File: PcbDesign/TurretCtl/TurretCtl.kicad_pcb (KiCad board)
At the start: 4 copper layers, 69.6 x 54.4 mm, 28 parts, among them J1 FLIR, J2 Stepper1, J3 Stepper2, J4 PWR

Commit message: Stepper Control Board V2
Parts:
- added D10: LED, LED_SMD:LED_0603_1608Metric, F.Cu at (29.2, 92.7)
- added D11: LED, LED_SMD:LED_0603_1608Metric, F.Cu at (79.0, 85.3)
- added D12: LED, LED_SMD:LED_0603_1608Metric, F.Cu at (29.2, 89.2)
- added D13: LED, LED_SMD:LED_0603_1608Metric, F.Cu at (79.0, 88.9)
- added D14: LED, LED_SMD:LED_0603_1608Metric, F.Cu at (52.6, 104.6)
- added D15: LED, LED_SMD:LED_0603_1608Metric, F.Cu at (69.1, 69.8)
- added D16: LED, LED_SMD:LED_0603_1608Metric, F.Cu at (29.2, 91.0)
- added D17: LED, LED_SMD:LED_0603_1608Metric, F.Cu at (79.0, 87.1)
- added D18: LED, LED_SMD:LED_0603_1608Metric, F.Cu at (69.1, 72.4)
- added D19: LED, LED_SMD:LED_0603_1608Metric, F.Cu at (69.1, 74.9)
- added D2: LED, LED_SMD:LED_0603_1608Metric, F.Cu at (52.3, 83.8)
- added D3: LED, LED_SMD:LED_0603_1608Metric, F.Cu at (55.6, 94.2)
- added D4: LED, LED_SMD:LED_0603_1608Metric, F.Cu at (52.3, 87.1)
- added D5: LED, LED_SMD:LED_0603_1608Metric, F.Cu at (55.6, 90.9)
- added D6: LED, LED_SMD:LED_0603_1608Metric, F.Cu at (52.3, 90.9)
- added D7: LED, LED_SMD:LED_0603_1608Metric, F.Cu at (55.6, 87.1)
- added D8: LED, LED_SMD:LED_0603_1608Metric, F.Cu at (52.3, 94.2)
- added D9: LED, LED_SMD:LED_0603_1608Metric, F.Cu at (55.6, 83.8)
- added J5: Sensors, Connector_JST:JST_GH_SM06B-GHS-TB_1x06-1MP_P1.25mm_Horizontal, F.Cu at (76.1, 72.5)
- added R10: 330, Resistor_SMD:R_0402_1005Metric, F.Cu at (52.3, 92.5)
- added R11: 330, Resistor_SMD:R_0402_1005Metric, F.Cu at (55.6, 88.6)
- added R12: 330, Resistor_SMD:R_0402_1005Metric, F.Cu at (52.3, 95.8)
- added R13: 330, Resistor_SMD:R_0402_1005Metric, F.Cu at (55.6, 85.3)
- added R14: 330, Resistor_SMD:R_0402_1005Metric, F.Cu at (26.4, 92.7)
- added R15: 330, Resistor_SMD:R_0402_1005Metric, F.Cu at (81.8, 85.3)
- added R16: 330, Resistor_SMD:R_0402_1005Metric, F.Cu at (26.4, 89.2)
- added R17: 330, Resistor_SMD:R_0402_1005Metric, F.Cu at (81.8, 88.9)
- added R18: 330, Resistor_SMD:R_0402_1005Metric, F.Cu at (52.6, 101.1)
- added R19: 330, Resistor_SMD:R_0402_1005Metric, F.Cu at (65.5, 69.8)
- added R20: 330, Resistor_SMD:R_0402_1005Metric, F.Cu at (26.4, 91.0)
- added R21: 330, Resistor_SMD:R_0402_1005Metric, F.Cu at (81.8, 87.1)
- added R22: 330, Resistor_SMD:R_0402_1005Metric, F.Cu at (65.5, 72.4)
- added R23: 330, Resistor_SMD:R_0402_1005Metric, F.Cu at (65.5, 74.9)
- added R6: 330, Resistor_SMD:R_0402_1005Metric, F.Cu at (52.3, 85.3)
- added R7: 330, Resistor_SMD:R_0402_1005Metric, F.Cu at (55.6, 95.8)
- added R8: 330, Resistor_SMD:R_0402_1005Metric, F.Cu at (52.3, 88.6)
- added R9: 330, Resistor_SMD:R_0402_1005Metric, F.Cu at (55.6, 92.5)
- R5: value 290 -> 330
- moved C15 98.9 mm to (36.1, 75.4)
- moved J1 97.7 mm to (46.9, 72.3)
- moved R1 73.5 mm to (26.9, 85.6), turned to 90 degrees
- moved C7 71.1 mm to (42.8, 103.1), turned to 180 degrees
- moved J3 70.7 mm to (61.0, 83.8), turned to -90 degrees
- moved R2 70.4 mm to (28.2, 85.6), turned to -90 degrees
- moved C8 66.6 mm to (30.7, 85.6), turned to 90 degrees
- moved C3 66.2 mm to (39.4, 94.3), turned to 180 degrees
- moved J2 65.7 mm to (47.0, 94.3), turned to 90 degrees
- moved U2 64.6 mm to (35.6, 89.2), turned to 180 degrees
- moved C9 63.8 mm to (32.5, 83.6), turned to 90 degrees
- moved C4 62.5 mm to (40.7, 92.2), turned to 180 degrees
- moved C6 62.5 mm to (40.7, 91.0)
- moved C11 57.9 mm to (67.4, 93.3), turned to -90 degrees
- moved C1 57.2 mm to (68.8, 83.8)
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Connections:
- U1 pad 17: /Stepper2/DVDD -> +5V
- U1 pad 18: /Stepper2/DVDD -> +5V
- U1 pad 25: GND -> (no net)
- U2 pad 17: /Stepper1/DVDD -> +5V
- U2 pad 18: /Stepper1/DVDD -> +5V
- U2 pad 25: GND -> (no net)
- XA1 pad D6: unconnected-(XA1-PadD6) -> D6
- XA1 pad D7: unconnected-(XA1-PadD7) -> D7
- XA1 pad D8: unconnected-(XA1-PadD8) -> D8
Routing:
- net +5V: track 33.9 -> 176.6 mm, vias 0 -> 12
- net SCL: track 72.9 -> 10.5 mm, vias 1 -> 0
- net SDA: track 70.4 -> 9.09 mm, vias 1 -> 0
- net GND: track 36.9 -> 67.2 mm, vias 36 -> 41
- net D8: track 0.00 -> 25.2 mm
- net D7: track 0.00 -> 24.4 mm
- net S2_DIR: track 43.5 -> 28.0 mm, vias 0 -> 1
- net S2_STEP: track 42.5 -> 30.4 mm, vias 0 -> 1
- net D6: track 0.00 -> 11.5 mm
- net /Stepper1/DVDD: track 23.7 -> 33.2 mm, vias 3 -> 0
- net /Stepper2/DVDD: track 23.7 -> 33.0 mm, vias 3 -> 0
- net +12V: track 21.5 -> 30.2 mm
- net S1_STEP: track 59.2 -> 56.0 mm, vias 0 -> 1
- net /Stepper2/RREF: track 3.58 -> 6.36 mm
- net /Stepper1/RREF: track 3.58 -> 6.36 mm
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- added copper zone on B.Cu, net +5V
- added copper zone on F.Cu, net +5V
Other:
- board size 69.6 x 54.4 mm -> 70.4 x 53.8 mm
- board text added: "12V"
- board text added: "5V"
- board text added: "DVDD ENABLE SLEEP"
- board text added: "GND"
- board text added: "LIDAR"
- board text added: "SLEEP ENABLE DVDD"
- board text added: "Sensor1"
- board text added: "Sensor2"
- board text added: "Sensor3"
- board text added: "Sensors"
- board text added: "Stepper Control Board V2 JLCJLCJLCJLC"
- board text added: "s1dir"
- board text added: "s1step"
- board text added: "s2dir"
- board text added: "s2step"
- board text removed: "-"
- board text removed: "A1A2B2B1"
- board text removed: "JLCJLCJLCJLC"
- board text removed: "PWR"
- board text removed: "SCL"
- board text removed: "SDA"
- board text removed: "Sense"
- board text removed: "Stepper Control Board V1"
- board text removed: "V12"

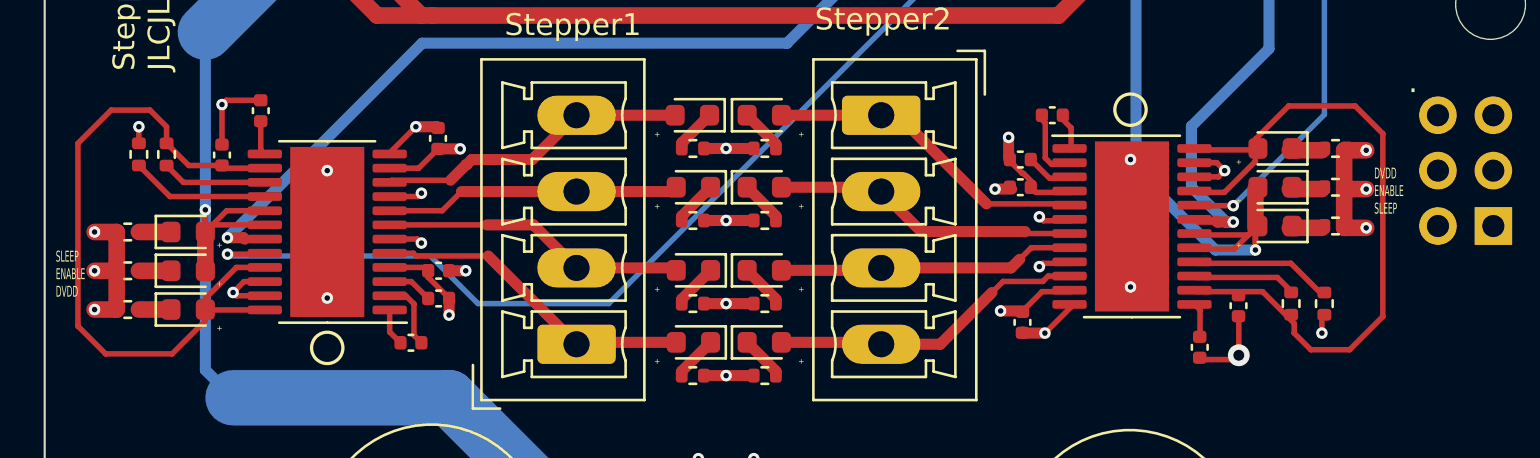
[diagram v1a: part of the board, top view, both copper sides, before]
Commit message: Removed dvdd leds
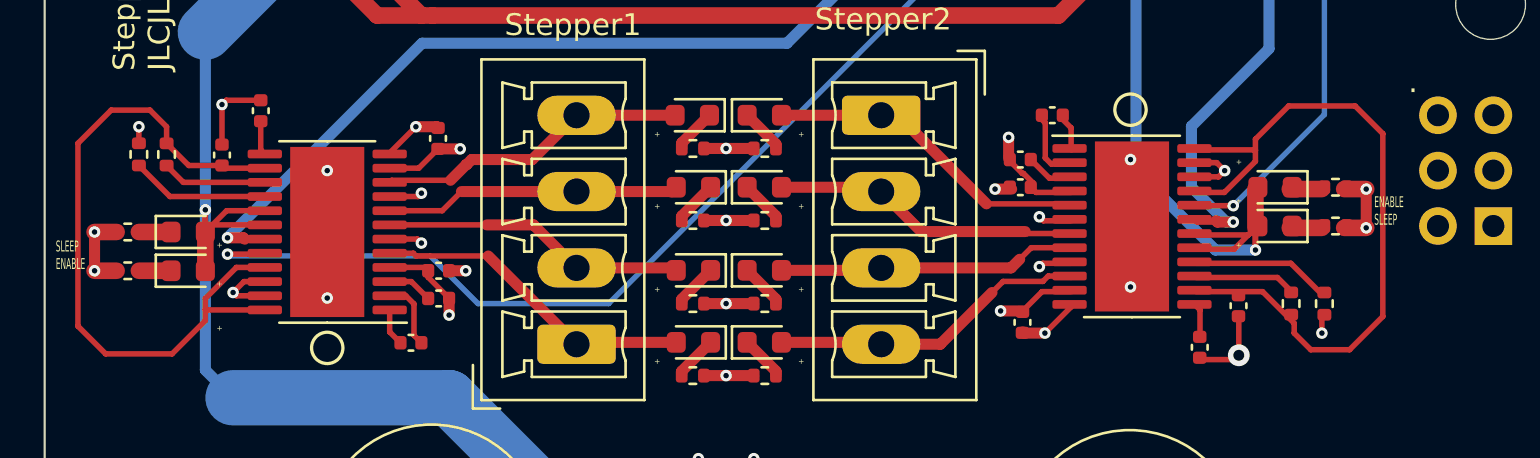
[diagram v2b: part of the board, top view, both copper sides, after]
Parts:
- removed D10, D11: LED, LED_SMD:LED_0603_1608Metric
- removed R14, R15: 330, Resistor_SMD:R_0402_1005Metric
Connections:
- U2 pad 25: (no net) -> GND
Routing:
- net GND: track 67.2 -> 61.6 mm, vias 41 -> 43
- net Net-(D11-K): track 1.47 -> 0.00 mm
- net Net-(D10-K): track 1.47 -> 0.00 mm
- net +5V: vias 12 -> 10
- net (no net): vias 2 -> 0
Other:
- board text added: "ENABLE SLEEP"
- board text added: "SLEEP ENABLE"
- board text removed: "DVDD ENABLE SLEEP"
- board text removed: "SLEEP ENABLE DVDD"

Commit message: New connectors
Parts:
- added D10: LED, LED_SMD:LED_0603_1608Metric, F.Cu at (93.6, 58.3)
- added D11: LED, LED_SMD:LED_0603_1608Metric, F.Cu at (93.6, 60.9)
- added D20: LED, LED_SMD:LED_0603_1608Metric, F.Cu at (93.6, 63.5)
- added R14: 330, Resistor_SMD:R_0402_1005Metric, F.Cu at (97.0, 58.0)
- added R15: 330, Resistor_SMD:R_0402_1005Metric, F.Cu at (97.0, 60.0)
- added R24: 330, Resistor_SMD:R_0402_1005Metric, F.Cu at (97.0, 62.0)
- J1, J5: footprint Connector_JST:JST_GH_SM06B-GHS-TB_1x06-1MP_P1.25mm_Horizontal -> Connector_Phoenix_MC:PhoenixContact_MCV_1,5_6-G-3.5_1x06_P3.50mm_Vertical
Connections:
- U2 pad 25: GND -> (no net)

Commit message: New Layout
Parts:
- moved C9 103.4 mm to (125.9, 128.0), turned to 0 degrees
- moved C8 103.4 mm to (125.9, 126.0), turned to 0 degrees
- moved D16 101.7 mm to (122.5, 131.4)
- moved D12 101.4 mm to (122.5, 128.8)
- moved R20 101.3 mm to (119.0, 132.1), turned to 0 degrees
- moved R16 101.2 mm to (119.0, 130.1), turned to 0 degrees
- moved J2 97.9 mm to (144.8, 89.2)
- moved R1 97.6 mm to (119.0, 118.2), turned to 0 degrees
- moved R2 97.1 mm to (119.0, 120.2), turned to 0 degrees
- moved D9 93.5 mm to (122.5, 149.2)
- moved C5 93.0 mm to (125.9, 122.1), turned to 0 degrees
- moved D20 92.3 mm to (102.9, 155.3)
- moved C6 91.4 mm to (125.9, 124.1)
- moved R13 91.3 mm to (119.0, 151.1), turned to 0 degrees
- moved C4 89.7 mm to (125.9, 120.1), turned to 0 degrees
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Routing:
- net +5V: track 176.6 -> 3.18 mm, vias 10 -> 1
- net S1_DIR: track 60.6 -> 0.00 mm, vias 1 -> 0
- net S1_STEP: track 56.0 -> 0.00 mm, vias 1 -> 0
- net GND: track 61.6 -> 13.4 mm, vias 43 -> 5
- net /Stepper1/DVDD: track 33.2 -> 0.00 mm
- net S2_STEP: track 30.4 -> 1.48 mm
- net S2_DIR: track 28.0 -> 1.47 mm
- net D8: track 25.2 -> 0.00 mm
- net D7: track 24.4 -> 0.00 mm
- net +12V: track 30.2 -> 9.79 mm, vias 13 -> 1
- net S1_AOUT2: track 15.5 -> 0.00 mm
- net S1_AOUT1: track 14.9 -> 0.00 mm
- net S1_BOUT1: track 14.4 -> 0.00 mm
- net S2_AOUT2: track 15.6 -> 1.48 mm, vias 0 -> 1
- net /Stepper2/DVDD: track 33.0 -> 19.0 mm, vias 0 -> 4
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- removed copper zone on F.Cu, net +12V
- removed copper zone on B.Cu, net +5V
- removed copper zone on F.Cu, net +5V
- removed copper zone on F.Cu, net GND
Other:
- board outline removed
- board text removed: "+"
- board text removed: "12V"
- board text removed: "5V"
- board text removed: "ENABLE SLEEP"
- board text removed: "GND"
- board text removed: "LIDAR"
- board text removed: "SLEEP ENABLE"
- board text removed: "Sensor1"
- board text removed: "Sensor2"
- board text removed: "Sensor3"
- board text removed: "Sensors"
- board text removed: "Stepper Control Board V2 JLCJLCJLCJLC"
- board text removed: "Stepper1"
- board text removed: "Stepper2"
- board text removed: "s1dir"
- board text removed: "s1step"
- board text removed: "s2dir"
- board text removed: "s2step"

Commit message: Control board v3
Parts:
- added D21: LED, LED_SMD:LED_0603_1608Metric, F.Cu at (116.6, 93.2)
- added D22: LED, LED_SMD:LED_0603_1608Metric, F.Cu at (118.6, 93.2)
- added R25: 330, Resistor_SMD:R_0402_1005Metric, F.Cu at (116.6, 90.4)
- added R26: 330, Resistor_SMD:R_0402_1005Metric, F.Cu at (118.6, 90.4)
- moved D19 76.9 mm to (116.6, 77.0), turned to 90 degrees
- moved D18 74.8 mm to (118.6, 76.9), turned to 90 degrees
- moved D15 72.8 mm to (120.7, 76.9), turned to 90 degrees
- moved D20 71.9 mm to (118.6, 85.1), turned to 90 degrees
- moved C9 70.1 mm to (126.0, 57.9), turned to 90 degrees
- moved D17 70.1 mm to (112.5, 85.1), turned to 90 degrees
- moved D14 68.6 mm to (112.5, 77.0), turned to 90 degrees
- moved C8 68.1 mm to (124.7, 57.9), turned to 90 degrees
- moved R21 67.5 mm to (112.5, 87.9), turned to -90 degrees
- moved D13 67.2 mm to (114.6, 85.1), turned to 90 degrees
- moved D10 65.8 mm to (122.7, 76.9), turned to 90 degrees
- moved R17 65.4 mm to (114.6, 87.9), turned to -90 degrees
- moved D9 64.2 mm to (120.7, 85.1), turned to 90 degrees
- moved R13 63.3 mm to (120.7, 87.9), turned to -90 degrees
- moved R2 63.1 mm to (122.7, 57.2), turned to -90 degrees
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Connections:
- D10 pad 2: GND -> Net-(D10-A)
- D11 pad 2: SDA -> S2_STEP
- D20 pad 2: SCL -> S2_DIR
- XA1 pad D9: unconnected-(XA1-PadD9) -> Net-(D10-A)
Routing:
- net +5V: track 3.18 -> 162.2 mm, vias 1 -> 5
- net S1_DIR: track 0.00 -> 71.5 mm, vias 0 -> 2
- net S1_STEP: track 0.00 -> 69.6 mm, vias 0 -> 2
- net D8: track 0.00 -> 67.9 mm, vias 0 -> 1
- net D7: track 0.00 -> 59.9 mm, vias 0 -> 1
- net S1_BOUT1: track 0.00 -> 58.9 mm, vias 0 -> 1
- net GND: track 13.4 -> 71.4 mm, vias 5 -> 28
- net S2_STEP: track 1.48 -> 52.6 mm, vias 1 -> 2
- net S2_DIR: track 1.47 -> 52.4 mm, vias 1 -> 2
- net S1_BOUT2: track 0.00 -> 50.8 mm, vias 0 -> 1
- net D6: track 0.00 -> 49.3 mm, vias 0 -> 1
- net S1_AOUT2: track 0.00 -> 42.7 mm, vias 0 -> 1
- net S1_AOUT1: track 0.00 -> 34.8 mm, vias 0 -> 1
- net S2_BOUT1: track 1.46 -> 30.8 mm
- net S2_BOUT2: track 1.47 -> 29.7 mm
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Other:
- board outline added: 69.1 x 53.8 mm
- board text added: "+"
- board text added: "12V"
- board text added: "5V"
- board text added: "A1"
- board text added: "A2"
- board text added: "B1"
- board text added: "B2"
- board text added: "Dir"
- board text added: "Dist"
- board text added: "Ena"
- board text added: "GND"
- board text added: "Lidar"
- board text added: "Power --"
- board text added: "S1"
- board text added: "S2"
- board text added: "S3"
- board text added: "Sensors"
- board text added: "Sensors ----"
- board text added: "Slp"
- board text added: "Step"
- board text added: "Stepper 1"
- board text added: "Stepper 1 -"
- board text added: "Stepper 1 -------------------"
- board text added: "Stepper 2"
- board text added: "Stepper 2 -------------------"
- board text added: "Stepper Control Board V3 JLCJLCJLCJLC"

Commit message: V3 adjustments
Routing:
- net GND: track 71.4 -> 83.8 mm
- net +5V: track 162.2 -> 163.8 mm
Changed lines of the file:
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@@
     (effects (font (size 0.254 0.254) (thickness 0.0635)) (justify left bottom))
   )
-  (gr_text "Sensors" (at 112.776 63.754 270) (layer "F.SilkS")
+  (gr_text "Sensors" (at 112.776 64.262 270) (layer "F.SilkS")
     (effects (font (size 0.508 0.508) (thickness 0.127)) (justify left))
   )
@@
     (effects (font (size 0.254 0.254) (thickness 0.0635)) (justify left bottom))
   )
-  (gr_text "Lidar" (at 112.776 53.594 270) (layer "F.SilkS")
+  (gr_text "Lidar" (at 112.522 54.102 270) (layer "F.SilkS")
     (effects (font (size 0.508 0.508) (thickness 0.127)) (justify left))
   )
@@
     (effects (font (size 0.254 0.254) (thickness 0.0635)) (justify left bottom))
   )
-  (gr_text "Stepper Control Board V3\nJLCJLCJLCJLC" (at 149.352 89.154 90) (layer "F.SilkS")
+  (gr_text "Stepper Control Board V3\nJLCJLCJLCJLC" (at 149.352 91.186 90) (layer "F.SilkS")
     (effects (font (size 1 1) (thickness 0.15)) (justify left bottom))
   )
@@
   (segment (start 119.5552 70.3377) (end 119.6392 70.4217) (width 0.254) (layer "F.Cu") (net 7))
   (segment (start 121.5872 66.3832) (end 121.5872 69.4337) (width 0.254) (layer "F.Cu") (net 8))
+  (segment (start 120.904 69.54) (end 122.7432 69.54) (width 0.254) (layer "F.Cu") (net 8))
   (segment (start 121.6002 66.3702) (end 121.5872 66.3832) (width 0.254) (layer "F.Cu") (net 8))
   (segment (start 112.522 89.154) (end 126.492 89.154) (width 0.508) (layer "F.Cu") (net 8))
@@
   (segment (start 125.4812 68.6437) (end 126.1872 68.6437) (width 0.508) (layer "F.Cu") (net 8))
   (segment (start 120.65 80.268) (end 120.65 81.026) (width 0.508) (layer "F.Cu") (net 8))
+  (segment (start 122.7432 69.54) (end 123.7032 68.58) (width 0.254) (layer "F.Cu") (net 8))
   (segment (start 139.375 66.3625) (end 139.362 66.3755) (width 0.254) (layer "F.Cu") (net 8))
   (segment (start 120.3827 56.6457) (end 120.3787 56.6497) (width 0.508) (layer "F.Cu") (net 8))
@@
   (segment (start 126.1872 68.6437) (end 126.2432 68.5877) (width 0.508) (layer "F.Cu") (net 8))
   (segment (start 118.618 88.396) (end 118.618 89.912) (width 0.508) (layer "F.Cu") (net 8))
+  (segment (start 140.462 69.596) (end 141.478 68.58) (width 0.254) (layer "F.Cu") (net 8))
   (segment (start 112.522 80.268) (end 112.522 81.077) (width 0.508) (layer "F.Cu") (net 8))
+  (segment (start 138.684 69.596) (end 140.462 69.596) (width 0.254) (layer "F.Cu") (net 8))
   (segment (start 143.256 68.636) (end 143.962 68.636) (width 0.508) (layer "F.Cu") (net 8))
   (segment (start 137.16 59.257215) (end 137.16 59.182) (width 0.254) (layer "F.Cu") (net 8))
@@
   (via (at 118.618 81.026) (size 0.53) (drill 0.25) (layers "F.Cu" "B.Cu") (free) (net 8))
   (via (at 116.586 89.154) (size 0.53) (drill 0.25) (layers "F.Cu" "B.Cu") (free) (net 8))
+  (segment (start 138.1535 56.642) (end 137.16 57.6355) (width 0.254) (layer "In1.Cu") (net 8))
+  (segment (start 119.3852 57.6432) (end 119.3852 59.1897) (width 0.254) (layer "In1.Cu") (net 8))
+  (segment (start 137.16 57.6355) (end 137.16 59.182) (width 0.254) (layer "In1.Cu") (net 8))
+  (segment (start 120.3787 56.6497) (end 119.3852 57.6432) (width 0.254) (layer "In1.Cu") (net 8))
   (segment (start 118.3692 59.1897) (end 118.3692 60.6262) (width 0.254) (layer "F.Cu") (net 9))
   (segment (start 120.3002 60.6452) (end 120.3002 59.3427) (width 0.254) (layer "F.Cu") (net 9))
@@
   (segment (start 143.275 60.6375) (end 143.275 58.909) (width 0.254) (layer "F.Cu") (net 12))
   (segment (start 143.275 58.909) (end 143.764 58.42) (width 0.254) (layer "F.Cu") (net 12))
-  (segment (start 122.245 59.3779) (end 122.4332 59.1897) (width 0.254) (layer "F.Cu") (net 13))
+  (segment (start 122.4332 59.1897) (end 122.4332 60.1757) (width 0.254) (layer "F.Cu") (net 13))
   (segment (start 140.208 60.1745) (end 140.671 60.6375) (width 0.508) (layer "F.Cu") (net 13))
   (segment (start 140.208 59.182) (end 140.208 60.1745) (width 0.508) (layer "F.Cu") (net 13))
@@
   (segment (start 111.506 75.235) (end 112.522 76.251) (width 0.254) (layer "F.Cu") (net 13))
   (segment (start 114.554 94.031) (end 112.522 94.031) (width 0.508) (layer "F.Cu") (net 13))
+  (segment (start 122.4332 60.1757) (end 122.895 60.6375) (width 0.254) (layer "F.Cu") (net 13))
   (segment (start 114.554 84.277) (end 112.522 84.277) (width 0.508) (layer "F.Cu") (net 13))
+  (segment (start 122.4332 59.1897) (end 122.245 59.3779) (width 0.254) (layer "F.Cu") (net 13))
   (segment (start 122.895 60.6375) (end 122.245 60.6375) (width 0.254) (layer "F.Cu") (net 13))
   (via (at 122.4332 59.1897) (size 0.53) (drill 0.25) (layers "F.Cu" "B.Cu") (free) (net 13))
